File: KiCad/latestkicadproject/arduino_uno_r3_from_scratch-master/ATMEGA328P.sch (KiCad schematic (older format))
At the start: 9 parts, among them IC5 ATMEGA328P-MU, SW1 RESET_SWITCH, Y2 Crystal

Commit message: PCB routing v1
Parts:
- C4, C6: footprint Capacitor_SMD:C_0805_2012Metric -> Capacitors_SMD:C_0805
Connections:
- net GND: now also SW1.1, SW1.2; no longer ICSP2.6 (P6)
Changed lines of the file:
@@
 LIBS:degson
 LIBS:PHT6NQ10T_135
+LIBS:L298P
 EELAYER 25 0
 EELAYER END
@@
 Text HLabel 4950 2975 0    40   Input ~ 0
 AREF
-Wire Wire Line
-	4950 2975 6000 2975
-Wire Wire Line
-	5250 2975 5250 3225
-Connection ~ 5250 2975
-Wire Wire Line
-	5250 3525 5250 3775
 $Comp
 L CONN_02X03 ICSP2
@@
 	1    0    0    -1
 $EndComp
-Wire Wire Line
-	4350 950  4350 1100
-Wire Wire Line
-	4050 950  4350 950
-Wire Wire Line
-	3200 950  3550 950
-Wire Wire Line
-	3200 850  3550 850
-Wire Wire Line
-	3200 750  3550 750
-Wire Wire Line
-	4050 850  4300 850
-Connection ~ 3200 1500
 $Comp
 L RESET_SWITCH SW1
@@
 	0    -1   -1   0
 $EndComp
-Wire Wire Line
-	2750 1500 2750 1650
-Connection ~ 2750 1500
-Wire Wire Line
-	2750 2275 2750 2425
-Connection ~ 2750 1650
-Connection ~ 2750 2275
-Wire Wire Line
-	3200 950  3200 1625
-Wire Wire Line
-	9900 3350 10850 3350
-Wire Wire Line
-	10450 3000 10450 3350
-Wire Wire Line
-	10450 2350 10450 2700
-Wire Wire Line
-	9900 2350 10825 2350
 $Comp
 L C C4
@@
 F 0 "C4" H 5300 3475 40  0000 L CNN
 F 1 "0.1 uF" H 5300 3275 40  0000 L CNN
-F 2 "Capacitor_SMD:C_0805_2012Metric" H 5288 3225 30  0000 C CNN
+F 2 "Capacitors_SMD:C_0805" H 5288 3225 30  0000 C CNN
 F 3 "http://images.ihscontent.net/vipimages/VipMasterIC/IC/KEME/KEMES10043/KEMES10043-1.pdf" H 5250 3375 60  0001 C CNN
 F 4 "CAPACITOR, CERAMIC, MULTILAYER, 100 V, X7R, 0.1 uF, SURFACE MOUNT, 0805, CHIP, ROHS COMPLIANT" H 5250 3375 60  0001 C CNN "Characteristics"
@@
 F 0 "C6" H 4500 4625 40  0000 L CNN
 F 1 "0.1 uF" H 4500 4425 40  0000 L CNN
-F 2 "Capacitor_SMD:C_0805_2012Metric" H 4488 4375 30  0000 C CNN
+F 2 "Capacitors_SMD:C_0805" H 4488 4375 30  0000 C CNN
 F 3 "http://images.ihscontent.net/vipimages/VipMasterIC/IC/KEME/KEMES10043/KEMES10043-1.pdf" H 4450 4525 60  0001 C CNN
 F 4 "CAPACITOR, CERAMIC, MULTILAYER, 100 V, X7R, 0.1 uF, SURFACE MOUNT, 0805, CHIP, ROHS COMPLIANT" H 4450 4525 60  0001 C CNN "Characteristics"
@@
 	-1   0    0    1
 $EndComp
-Wire Wire Line
-	2850 1650 2850 1775
-Wire Wire Line
-	2650 1650 2850 1650
-Wire Wire Line
-	2650 1775 2650 1650
-Wire Wire Line
-	2850 2275 2850 2175
-Wire Wire Line
-	2650 2275 2850 2275
-Wire Wire Line
-	2650 2275 2650 2175
-$Comp
-L GND-RESCUE-Arduino_Uno_R3_From_Scratch #PWR026
+$Comp
+L GND-RESCUE-Arduino_Uno_R3_From_Scratch #PWR029
 U 1 1 562077A6
 P 5250 3775
-F 0 "#PWR026" H 5250 3775 30  0001 C CNN
+F 0 "#PWR029" H 5250 3775 30  0001 C CNN
 F 1 "GND" H 5250 3705 30  0001 C CNN
 F 2 "~" H 5250 3775 60  0000 C CNN
@@
 F 6 "~" H 5250 3775 60  0001 C CNN "Notes"
 	1    5250 3775
-	1    0    0    -1
-$EndComp
-$Comp
-L GND-RESCUE-Arduino_Uno_R3_From_Scratch #PWR027
-U 1 1 562079B8
-P 2750 2425
-F 0 "#PWR027" H 2750 2425 30  0001 C CNN
-F 1 "GND" H 2750 2355 30  0001 C CNN
-F 2 "~" H 2750 2425 60  0000 C CNN
-F 3 "~" H 2750 2425 60  0000 C CNN
-F 4 "ANY" H 2750 2425 60  0001 C CNN "Source"
-F 5 "N" H 2750 2425 60  0001 C CNN "Critical"
-F 6 "~" H 2750 2425 60  0001 C CNN "Notes"
-	1    2750 2425
-	1    0    0    -1
-$EndComp
-$Comp
-L GND-RESCUE-Arduino_Uno_R3_From_Scratch #PWR028
-U 1 1 56208C49
-P 4350 1100
-F 0 "#PWR028" H 4350 1100 30  0001 C CNN
-F 1 "GND" H 4350 1030 30  0001 C CNN
-F 2 "~" H 4350 1100 60  0000 C CNN
-F 3 "~" H 4350 1100 60  0000 C CNN
-F 4 "ANY" H 4350 1100 60  0001 C CNN "Source"
-F 5 "N" H 4350 1100 60  0001 C CNN "Critical"
-F 6 "~" H 4350 1100 60  0001 C CNN "Notes"
-	1    4350 1100
 	1    0    0    -1
 $EndComp
@@
 NoConn ~ 6000 3825
 NoConn ~ 6000 3725
-Wire Wire Line
-	9900 2350 9900 2975
-Wire Wire Line
-	7900 3075 9900 3075
-Wire Wire Line
-	9900 3075 9900 3350
-Wire Wire Line
-	9900 2975 7900 2975
 Text HLabel 3200 750  0    60   Input ~ 0
 DIRA
@@
 Text HLabel 7900 4675 2    60   Input ~ 0
 IO7
-Wire Wire Line
-	7900 3825 8750 3825
-Connection ~ 8400 3825
-$Comp
-L +5V #PWR029
+$Comp
+L +5V #PWR030
 U 1 1 5AA163DD
 P 8400 3500
-F 0 "#PWR029" H 8400 3350 50  0001 C CNN
+F 0 "#PWR030" H 8400 3350 50  0001 C CNN
 F 1 "+5V" H 8400 3640 50  0000 C CNN
 F 2 "" H 8400 3500 50  0001 C CNN
@@
 	1    0    0    -1
 $EndComp
-Wire Wire Line
-	8400 3800 8400 3825
-Wire Wire Line
-	3200 1500 2750 1500
 Text HLabel 3200 1625 3    60   Input ~ 0
 RESET
-Wire Wire Line
-	4050 750  4350 750
-Wire Wire Line
-	4350 750  4350 725
-$Comp
-L +5V #PWR030
+$Comp
+L +5V #PWR031
 U 1 1 5AA16A11
 P 4350 725
-F 0 "#PWR030" H 4350 575 50  0001 C CNN
+F 0 "#PWR031" H 4350 575 50  0001 C CNN
 F 1 "+5V" H 4350 865 50  0000 C CNN
 F 2 "" H 4350 725 50  0001 C CNN
@@
 	1    0    0    -1
 $EndComp
-Wire Wire Line
-	6000 4475 6000 4675
-Wire Wire Line
-	6000 4675 4325 4675
-Wire Wire Line
-	4325 4675 4325 4750
-Connection ~ 4450 4675
-$Comp
-L GND #PWR031
+$Comp
+L GND #PWR032
 U 1 1 5AA16DB8
 P 4325 4750
-F 0 "#PWR031" H 4325 4500 50  0001 C CNN
+F 0 "#PWR032" H 4325 4500 50  0001 C CNN
 F 1 "GND" H 4325 4600 50  0000 C CNN
 F 2 "" H 4325 4750 50  0001 C CNN
@@
 	1    0    0    -1
 $EndComp
-Connection ~ 6000 4575
-Wire Wire Line
-	6000 2375 6000 2675
-Wire Wire Line
-	6000 2375 4450 2375
-Wire Wire Line
-	4450 2375 4450 4375
-Wire Wire Line
-	4450 4225 4200 4225
-Wire Wire Line
-	4200 4225 4200 4150
-Connection ~ 4450 4225
-$Comp
-L +5V #PWR032
+$Comp
+L +5V #PWR033
 U 1 1 5AA170DA
 P 4200 4150
-F 0 "#PWR032" H 4200 4000 50  0001 C CNN
+F 0 "#PWR033" H 4200 4000 50  0001 C CNN
 F 1 "+5V" H 4200 4290 50  0000 C CNN
 F 2 "" H 4200 4150 50  0001 C CNN
@@
 	1    0    0    -1
 $EndComp
-Connection ~ 6000 2475
-Text HLabel 4350 950  2    60   Input ~ 0
-GND
 $Comp
 L Crystal Y2
@@
 	0    1    1    0
 $EndComp
-Wire Wire Line
-	10825 2350 10825 2450
-Connection ~ 10450 2350
-Wire Wire Line
-	10850 3350 10850 3250
-Connection ~ 10450 3350
 $Comp
 L C C5
@@
 $EndComp
 $Comp
-L GND #PWR033
+L GND #PWR034
 U 1 1 5AA900E3
 P 10825 2750
-F 0 "#PWR033" H 10825 2500 50  0001 C CNN
+F 0 "#PWR034" H 10825 2500 50  0001 C CNN
 F 1 "GND" H 10825 2600 50  0000 C CNN
 F 2 "" H 10825 2750 50  0001 C CNN
@@
 $EndComp
 $Comp
-L GND #PWR034
+L GND #PWR035
 U 1 1 5AA90124
 P 10850 2950
-F 0 "#PWR034" H 10850 2700 50  0001 C CNN
+F 0 "#PWR035" H 10850 2700 50  0001 C CNN
 F 1 "GND" H 10850 2800 50  0000 C CNN
 F 2 "" H 10850 2950 50  0001 C CNN
@@
 	0    -1   -1   0
 $EndComp
+Wire Wire Line
+	4950 2975 6000 2975
+Wire Wire Line
+	5250 2975 5250 3225
+Connection ~ 5250 2975
+Wire Wire Line
+	5250 3525 5250 3775
+Wire Wire Line
+	4350 950  4350 1100
+Wire Wire Line
+	4050 950  4350 950
+Wire Wire Line
+	3200 950  3550 950
+Wire Wire Line
+	3200 850  3550 850
+Wire Wire Line
+	3200 750  3550 750
+Wire Wire Line
+	4050 850  4300 850
+Connection ~ 3200 1500
+Wire Wire Line
+	2750 1500 2750 1650
+Connection ~ 2750 1500
+Connection ~ 2750 1650
+Wire Wire Line
+	3200 950  3200 1625
+Wire Wire Line
+	9900 3350 10850 3350
+Wire Wire Line
+	10450 3000 10450 3350
+Wire Wire Line
+	10450 2350 10450 2700
+Wire Wire Line
+	9900 2350 10825 2350
+Wire Wire Line
+	2850 1650 2850 1775
+Wire Wire Line
+	2650 1650 2850 1650
+Wire Wire Line
+	2650 1775 2650 1650
+Wire Wire Line
+	2850 2275 2850 2175
+Wire Wire Line
+	2650 2275 2650 2175
+Wire Wire Line
+	9900 2350 9900 2975
+Wire Wire Line
+	7900 3075 9900 3075
+Wire Wire Line
+	9900 3075 9900 3350
+Wire Wire Line
+	9900 2975 7900 2975
+Wire Wire Line
+	7900 3825 8750 3825
+Connection ~ 8400 3825
+Wire Wire Line
+	8400 3800 8400 3825
+Wire Wire Line
+	3200 1500 2750 1500
+Wire Wire Line
+	4050 750  4350 750
+Wire Wire Line
+	4350 750  4350 725
+Wire Wire Line
+	6000 4475 6000 4675
+Wire Wire Line
+	6000 4675 4325 4675
+Wire Wire Line
+	4325 4675 4325 4750
+Connection ~ 4450 4675
+Connection ~ 6000 4575
+Wire Wire Line
+	6000 2375 6000 2675
+Wire Wire Line
+	6000 2375 4450 2375
+Wire Wire Line
+	4450 2375 4450 4375
+Wire Wire Line
+	4450 4225 4200 4225
+Wire Wire Line
+	4200 4225 4200 4150
+Connection ~ 4450 4225
+Connection ~ 6000 2475
+Wire Wire Line
+	10825 2350 10825 2450
+Connection ~ 10450 2350
+Wire Wire Line
+	10850 3350 10850 3250
+Connection ~ 10450 3350
+$Comp
+L GND-RESCUE-Arduino_Uno_R3_From_Scratch #PWR036
+U 1 1 56208C49
+P 4350 1100
+F 0 "#PWR036" H 4350 1100 30  0001 C CNN
+F 1 "GND" H 4350 1030 30  0001 C CNN
+F 2 "~" H 4350 1100 60  0000 C CNN
+F 3 "~" H 4350 1100 60  0000 C CNN
+F 4 "ANY" H 4350 1100 60  0001 C CNN "Source"
+F 5 "N" H 4350 1100 60  0001 C CNN "Critical"
+F 6 "~" H 4350 1100 60  0001 C CNN "Notes"
+	1    4350 1100
+	1    0    0    -1
+$EndComp
+Wire Wire Line
+	2650 2275 2850 2275
+Text HLabel 2750 2275 0    60   Input ~ 0
+GND
 $EndSCHEMATC

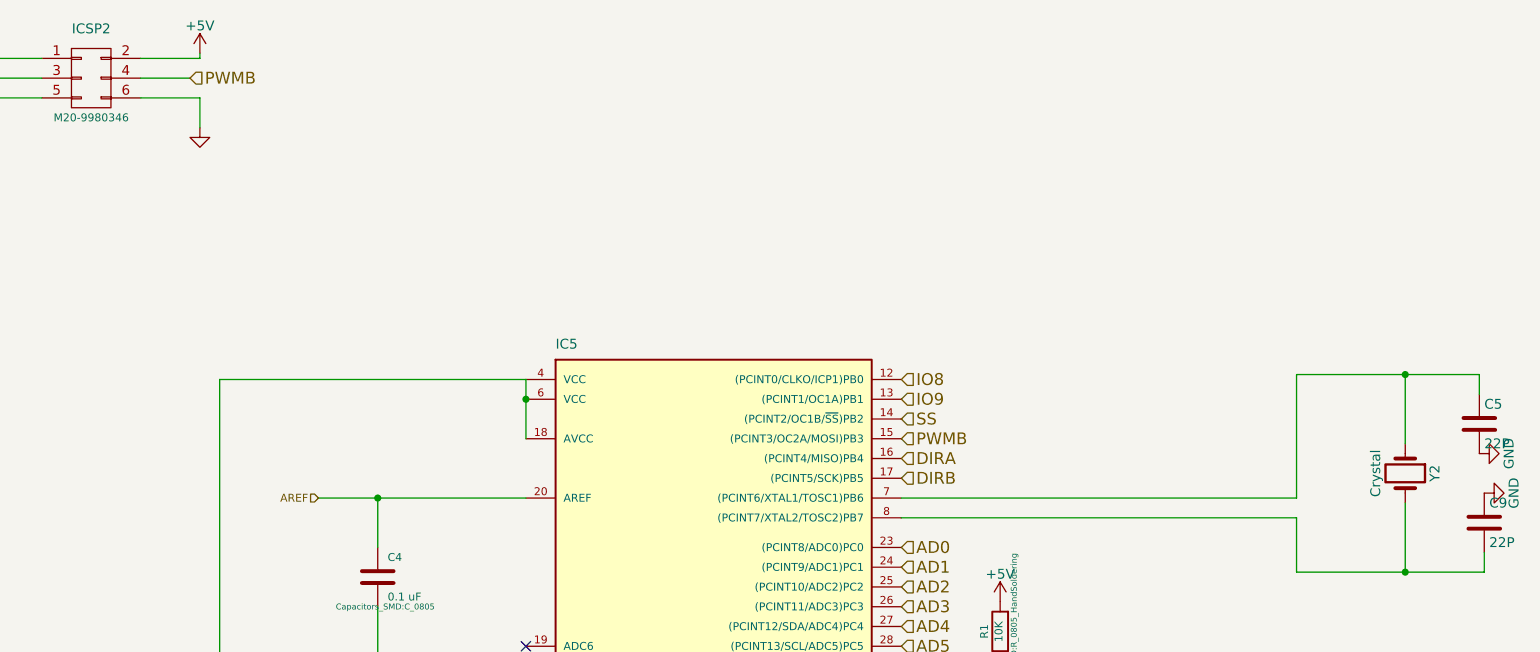
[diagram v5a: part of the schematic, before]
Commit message: correctie gnd-fouten
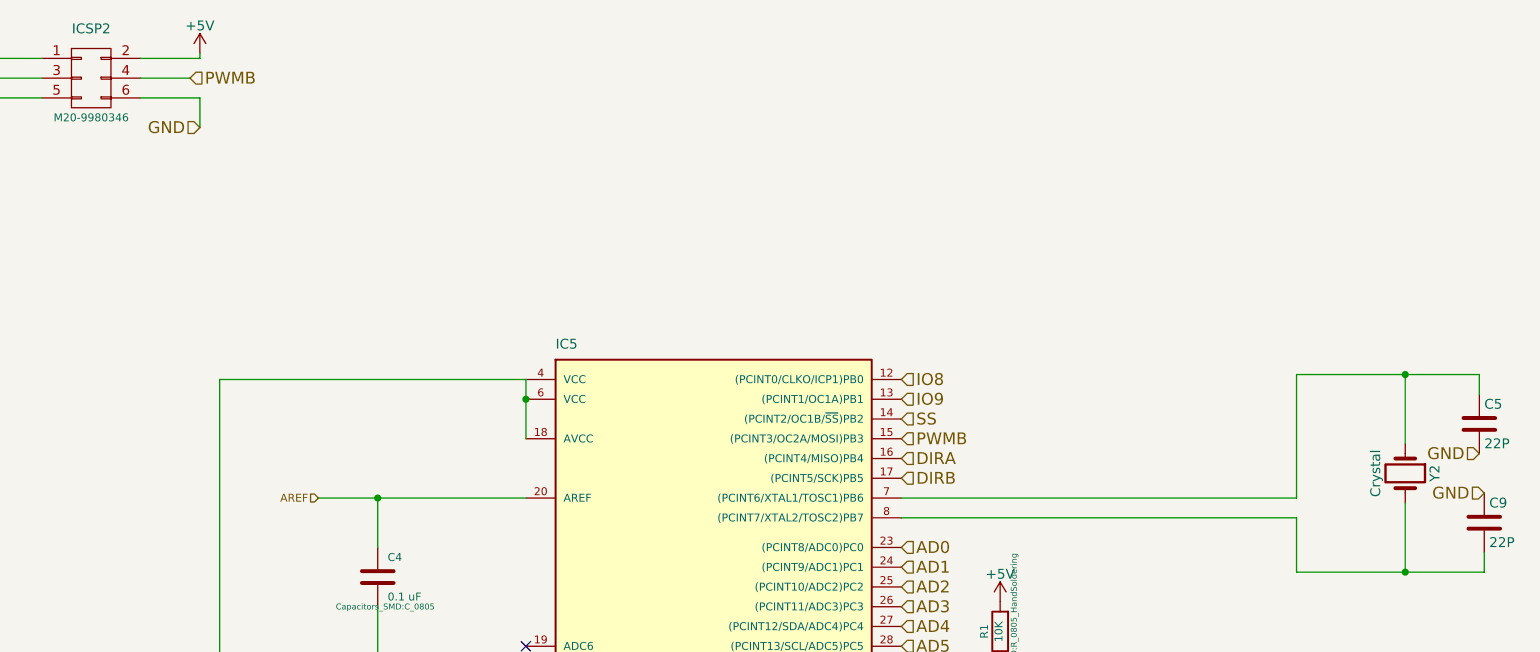
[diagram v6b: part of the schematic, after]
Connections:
- net GND: now also ICSP2.6 (P6)
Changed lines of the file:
@@
 $EndComp
 $Comp
-L GND-RESCUE-Arduino_Uno_R3_From_Scratch #PWR029
+L GND-RESCUE-Arduino_Uno_R3_From_Scratch #PWR025
 U 1 1 562077A6
 P 5250 3775
-F 0 "#PWR029" H 5250 3775 30  0001 C CNN
+F 0 "#PWR025" H 5250 3775 30  0001 C CNN
 F 1 "GND" H 5250 3705 30  0001 C CNN
 F 2 "~" H 5250 3775 60  0000 C CNN
@@
 IO7
 $Comp
-L +5V #PWR030
+L +5V #PWR026
 U 1 1 5AA163DD
 P 8400 3500
-F 0 "#PWR030" H 8400 3350 50  0001 C CNN
+F 0 "#PWR026" H 8400 3350 50  0001 C CNN
 F 1 "+5V" H 8400 3640 50  0000 C CNN
 F 2 "" H 8400 3500 50  0001 C CNN
@@
 RESET
 $Comp
-L +5V #PWR031
+L +5V #PWR027
 U 1 1 5AA16A11
 P 4350 725
-F 0 "#PWR031" H 4350 575 50  0001 C CNN
+F 0 "#PWR027" H 4350 575 50  0001 C CNN
 F 1 "+5V" H 4350 865 50  0000 C CNN
 F 2 "" H 4350 725 50  0001 C CNN
@@
 $EndComp
 $Comp
-L GND #PWR032
+L GND #PWR028
 U 1 1 5AA16DB8
 P 4325 4750
-F 0 "#PWR032" H 4325 4500 50  0001 C CNN
+F 0 "#PWR028" H 4325 4500 50  0001 C CNN
 F 1 "GND" H 4325 4600 50  0000 C CNN
 F 2 "" H 4325 4750 50  0001 C CNN
@@
 $EndComp
 $Comp
-L +5V #PWR033
+L +5V #PWR029
 U 1 1 5AA170DA
 P 4200 4150
-F 0 "#PWR033" H 4200 4000 50  0001 C CNN
+F 0 "#PWR029" H 4200 4000 50  0001 C CNN
 F 1 "+5V" H 4200 4290 50  0000 C CNN
 F 2 "" H 4200 4150 50  0001 C CNN
@@
 	1    0    0    -1
 $EndComp
-$Comp
-L GND #PWR034
-U 1 1 5AA900E3
-P 10825 2750
-F 0 "#PWR034" H 10825 2500 50  0001 C CNN
-F 1 "GND" H 10825 2600 50  0000 C CNN
-F 2 "" H 10825 2750 50  0001 C CNN
-F 3 "" H 10825 2750 50  0001 C CNN
-	1    10825 2750
-	0    -1   -1   0
-$EndComp
-$Comp
-L GND #PWR035
-U 1 1 5AA90124
-P 10850 2950
-F 0 "#PWR035" H 10850 2700 50  0001 C CNN
-F 1 "GND" H 10850 2800 50  0000 C CNN
-F 2 "" H 10850 2950 50  0001 C CNN
-F 3 "" H 10850 2950 50  0001 C CNN
-	1    10850 2950
-	0    -1   -1   0
-$EndComp
 Wire Wire Line
 	4950 2975 6000 2975
@@
 	10850 3350 10850 3250
 Connection ~ 10450 3350
-$Comp
-L GND-RESCUE-Arduino_Uno_R3_From_Scratch #PWR036
-U 1 1 56208C49
-P 4350 1100
-F 0 "#PWR036" H 4350 1100 30  0001 C CNN
-F 1 "GND" H 4350 1030 30  0001 C CNN
-F 2 "~" H 4350 1100 60  0000 C CNN
-F 3 "~" H 4350 1100 60  0000 C CNN
-F 4 "ANY" H 4350 1100 60  0001 C CNN "Source"
-F 5 "N" H 4350 1100 60  0001 C CNN "Critical"
-F 6 "~" H 4350 1100 60  0001 C CNN "Notes"
-	1    4350 1100
-	1    0    0    -1
-$EndComp
 Wire Wire Line
 	2650 2275 2850 2275
 Text HLabel 2750 2275 0    60   Input ~ 0
 GND
+Text HLabel 10850 2950 0    60   Input ~ 0
+GND
+Text HLabel 10825 2750 0    60   Input ~ 0
+GND
+Text HLabel 4350 1100 0    60   Input ~ 0
+GND
 $EndSCHEMATC

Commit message: verbeteringen kicad
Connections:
- net GND: now also C4.2
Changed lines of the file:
@@
-$EndComp
-$Comp
-L GND-RESCUE-Arduino_Uno_R3_From_Scratch #PWR025
-U 1 1 562077A6
-P 5250 3775
-F 0 "#PWR025" H 5250 3775 30  0001 C CNN
-F 1 "GND" H 5250 3705 30  0001 C CNN
-F 2 "~" H 5250 3775 60  0000 C CNN
-F 3 "~" H 5250 3775 60  0000 C CNN
-F 4 "ANY" H 5250 3775 60  0001 C CNN "Source"
-F 5 "N" H 5250 3775 60  0001 C CNN "Critical"
-F 6 "~" H 5250 3775 60  0001 C CNN "Notes"
-	1    5250 3775
-	1    0    0    -1
 $EndComp
 $Comp
@@
 IO7
 $Comp
-L +5V #PWR026
+L +5V #PWR025
 U 1 1 5AA163DD
 P 8400 3500
-F 0 "#PWR026" H 8400 3350 50  0001 C CNN
+F 0 "#PWR025" H 8400 3350 50  0001 C CNN
 F 1 "+5V" H 8400 3640 50  0000 C CNN
 F 2 "" H 8400 3500 50  0001 C CNN
@@
 RESET
 $Comp
-L +5V #PWR027
+L +5V #PWR026
 U 1 1 5AA16A11
 P 4350 725
-F 0 "#PWR027" H 4350 575 50  0001 C CNN
+F 0 "#PWR026" H 4350 575 50  0001 C CNN
 F 1 "+5V" H 4350 865 50  0000 C CNN
 F 2 "" H 4350 725 50  0001 C CNN
@@
 $EndComp
 $Comp
-L GND #PWR028
-U 1 1 5AA16DB8
-P 4325 4750
-F 0 "#PWR028" H 4325 4500 50  0001 C CNN
-F 1 "GND" H 4325 4600 50  0000 C CNN
-F 2 "" H 4325 4750 50  0001 C CNN
-F 3 "" H 4325 4750 50  0001 C CNN
-	1    4325 4750
-	1    0    0    -1
-$EndComp
-$Comp
-L +5V #PWR029
+L +5V #PWR027
 U 1 1 5AA170DA
 P 4200 4150
-F 0 "#PWR029" H 4200 4000 50  0001 C CNN
+F 0 "#PWR027" H 4200 4000 50  0001 C CNN
 F 1 "+5V" H 4200 4290 50  0000 C CNN
 F 2 "" H 4200 4150 50  0001 C CNN
@@
 Text HLabel 4350 1100 0    60   Input ~ 0
 GND
+Text HLabel 4325 4750 0    60   Input ~ 0
+GND
+Text HLabel 5250 3775 0    60   Input ~ 0
+GND
 $EndSCHEMATC

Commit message: PCBtotaal
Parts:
- SW1: footprint RESET_SWITCH:FSM4JSMATR -> 4-1437565-1:FSM-SWITCH
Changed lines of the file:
@@
 F 0 "SW1" V 2600 2275 60  0000 C CNN
 F 1 "RESET_SWITCH" V 2900 2525 60  0000 C CNN
-F 2 "RESET_SWITCH:FSM4JSMATR" H 2750 1975 60  0001 C CNN
+F 2 "4-1437565-1:FSM-SWITCH" H 2750 1975 60  0001 C CNN
 F 3 "http://industrial.panasonic.com/www-data/pdf/ATK0000/ATK0000CE28.pdf" H 2750 1975 60  0001 C CNN
 F 4 "SWITCH TACTILE SPST-NO 0.02A 15V" H 2750 1975 60  0001 C CNN "Characteristics"
@@
 IO7
 $Comp
-L +5V #PWR025
+L +5V #PWR07
 U 1 1 5AA163DD
 P 8400 3500
-F 0 "#PWR025" H 8400 3350 50  0001 C CNN
+F 0 "#PWR07" H 8400 3350 50  0001 C CNN
 F 1 "+5V" H 8400 3640 50  0000 C CNN
 F 2 "" H 8400 3500 50  0001 C CNN
@@
 RESET
 $Comp
-L +5V #PWR026
+L +5V #PWR08
 U 1 1 5AA16A11
 P 4350 725
-F 0 "#PWR026" H 4350 575 50  0001 C CNN
+F 0 "#PWR08" H 4350 575 50  0001 C CNN
 F 1 "+5V" H 4350 865 50  0000 C CNN
 F 2 "" H 4350 725 50  0001 C CNN
@@
 $EndComp
 $Comp
-L +5V #PWR027
+L +5V #PWR09
 U 1 1 5AA170DA
 P 4200 4150
-F 0 "#PWR027" H 4200 4000 50  0001 C CNN
+F 0 "#PWR09" H 4200 4000 50  0001 C CNN
 F 1 "+5V" H 4200 4290 50  0000 C CNN
 F 2 "" H 4200 4150 50  0001 C CNN
